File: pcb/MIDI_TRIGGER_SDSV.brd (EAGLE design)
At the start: 100 x 80 mm, 20 parts, among them IC1 AT90S2313P, IC7 7805TV, J1 DCJ0202

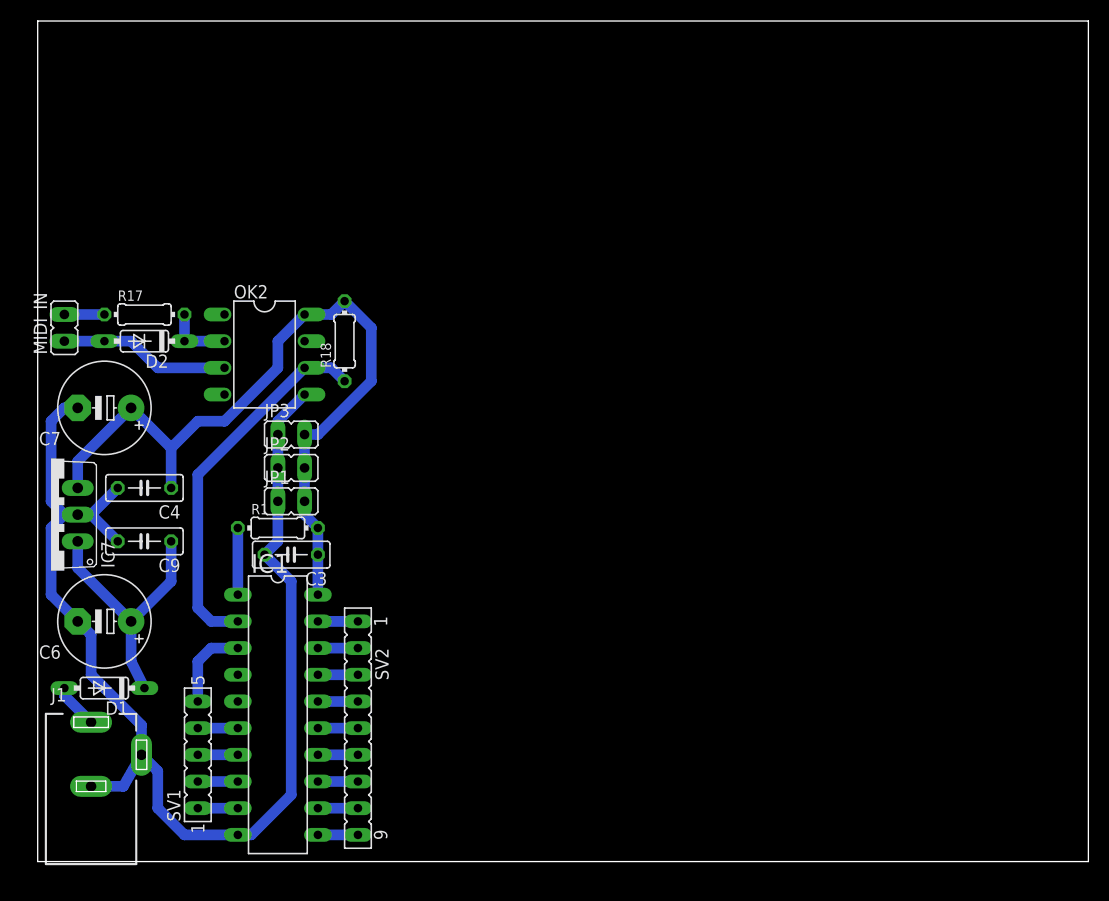
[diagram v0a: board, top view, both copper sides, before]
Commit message: updated schematic and added picture of schematic for non-eagle users
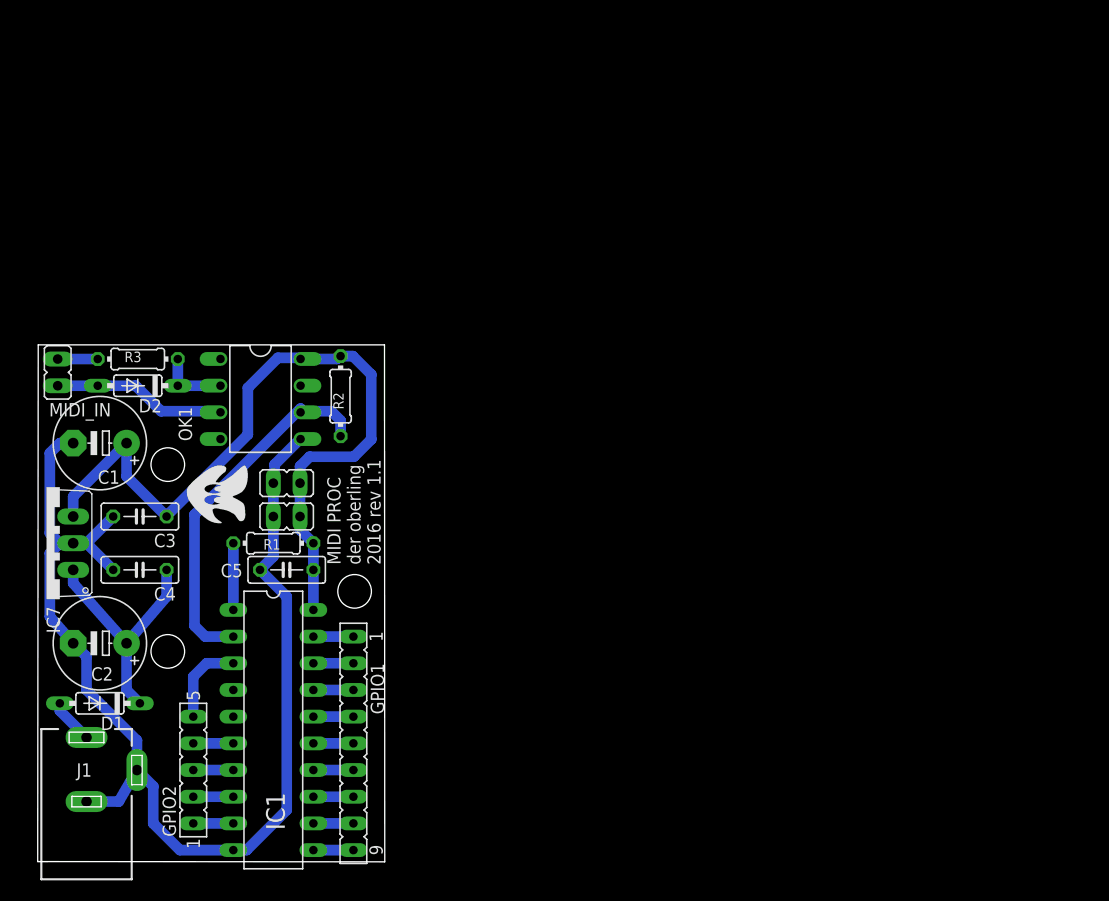
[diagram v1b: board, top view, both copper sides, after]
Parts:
- removed C6, C7: 10µF, resistor:E5-8,5
- removed C9: (no value), rcl:C050-025X075
- removed JP3: (no value), jumper:JP1
- removed OK2: 6N135, optocoupler:DIL08
- removed R17, R18: (no value), resistor:0204/7
- removed SV1: (no value), con-lsta:FE05-1
- removed SV2: (no value), con-lsta:FE09
- added C1, C2: 10µF, resistor:E5-8,5
- added C5: 100n, rcl:C050-025X075
- added GPIO1: (no value), con-lsta:FE09
- added GPIO2: (no value), con-lsta:FE05-1
- added OK1: 6N138, optocoupler:DIL08
- added R2: 360, resistor:0204/7
- added R3: 220, resistor:0204/7
- C3, C4: value (none) -> 100n
- D1, D2: value 1N4148DO35-7 -> 1N4148
- R1: value (none) -> 10k
- moved C3 14.9 mm to (9.73, 32.8)
- moved C4 7.81 mm to (9.73, 27.8)
- moved D2 4.29 mm to (9.53, 45.3)
- moved MIDI_IN 4.29 mm to (1.91, 46.6)
- moved IC7 2.75 mm to (0.84, 30.3)
- moved D1 1.51 mm to (5.92, 15.1)
- moved IC1 1.51 mm to (22.4, 12.5)
- moved J1 1.51 mm to (4.65, 8.71)
- moved JP1 1.51 mm to (23.7, 32.8)
- moved JP2 1.51 mm to (23.7, 36.0)
- moved R1 1.51 mm to (22.4, 30.3)
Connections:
- net 16V_DC_IN renamed 7.5-9V_DC_IN
- removed net N$8: IC1.13, SV2.7
- removed net N$9: IC1.12, SV2.8
- new net OUT7: GPIO1.2, IC1.18
- new net OUT8: GPIO1.1, IC1.19
- net GND: now also C1.-, C2.-, C5.2, OK1.5; no longer C6.-, C7.-, C9.2, JP3.1, OK2.5
- net MIDI_IN: now also OK1.6, R2.1; no longer OK2.6, R18.1
- net N$1: now also GPIO1.9; no longer SV2.9
- net N$2: now also GPIO2.1; no longer SV1.1
- net N$3: now also GPIO2.2; no longer SV1.2
- net N$31: now also R3.1; no longer R17.1
- net N$32: now also OK1.2, R3.2; no longer OK2.2, R17.2
- net N$33: now also OK1.3; no longer OK2.3
- net N$4: now also C2.+, C4.1; no longer C6.+, C9.1
- net N$5: now also GPIO2.3; no longer SV1.3
- net N$6: now also GPIO2.4; no longer SV1.4
- net N$7: now also GPIO2.5; no longer SV1.5
- net OUT1: now also GPIO1.8, IC1.12; no longer IC1.14, SV2.6
- net OUT2: now also GPIO1.7, IC1.13; no longer IC1.15, SV2.5
- net OUT3: now also GPIO1.6, IC1.14; no longer IC1.16, SV2.4
- net OUT4: now also GPIO1.5, IC1.15; no longer IC1.17, SV2.3
- net OUT5: now also GPIO1.4, IC1.16; no longer IC1.18, SV2.2
- net OUT6: now also GPIO1.3, IC1.17; no longer IC1.19, SV2.1
- net VCC: now also C1.+, C5.1, OK1.8, R2.2; no longer C4.1, C7.+, JP3.2, OK2.8, R18.2
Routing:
- net GND: track 117.5 -> 112.3 mm
- net OUT8: track 0.00 -> 3.81 mm
- net OUT7: track 0.00 -> 3.81 mm
- net N$9: track 3.81 -> 0.00 mm
- net N$8: track 3.81 -> 0.00 mm
- net N$4: track 25.6 -> 23.6 mm
- net MIDI_IN: track 35.7 -> 35.1 mm
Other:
- board size 100 x 80 mm -> 33 x 49.2 mm
- board text added: "/home/oberling/eagle/logo.bmp"
- board text added: "MIDI PROC der oberling 2016 rev 1.1"
